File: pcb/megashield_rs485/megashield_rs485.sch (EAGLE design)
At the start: 16 parts

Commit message: PCB template
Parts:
- removed JP10: (no value), SparkFun:M06LOCK
- removed JP11, JP12: (no value), SparkFun:M02LOCK
- removed JP3, JP4, JP5, JP6, JP7: (no value), SparkFun:M08LOCK
- removed JP8, JP9: M16LOCK, SparkFun:M16LOCK
- removed LED1: Red, SparkFun:LED5MM
- removed LED2: Green, SparkFun:LED5MM
- removed R1, R2: 330, SparkFun:RESISTORPTH1
- removed R3: 10k, SparkFun:RESISTORPTH1
- removed S1: (no value), SparkFun:TAC_SWITCHPTH
- added J1, J2, J3, J8, J9: (no value), mecatronica_eagle_lib:M08LONGPADS
- added J10: (no value), mecatronica_eagle_lib:M06LONGPADS
- added J4, J5: (no value), mecatronica_eagle_lib:M16PTH
- added J6, J7: (no value), mecatronica_eagle_lib:M02PTH
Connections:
- removed net GND: JP10.4, JP10.5, JP11.1, JP11.2, JP3.7, LED1.C, LED2.C, S1.1, S1.2
- removed net N$126: LED1.A, R1.1
- removed net N$127: LED2.A, R2.1
- new net ASD: J1.7, J10.4, J10.5, J7.1, J7.2
- net 3.3: now also J10.2; no longer JP10.2
- net 5V: now also J10.3; no longer JP10.3, R1.2, R3.2
- net 5V@1: now also J6.1, J6.2; no longer JP12.1, JP12.2
- net A0: now also J9.1; no longer JP7.1
- net A1: now also J9.2; no longer JP7.2
- net A10: now also J8.3; no longer JP6.3
- net A11: now also J8.4; no longer JP6.4
- net A12: now also J8.5; no longer JP6.5
- net A13: now also J8.6; no longer JP6.6
- net A14: now also J8.7; no longer JP6.7
- net A15: now also J8.8; no longer JP6.8
- net A2: now also J9.3; no longer JP7.3
- net A3: now also J9.4; no longer JP7.4
- net A4: now also J9.5; no longer JP7.5
- net A5: now also J9.6; no longer JP7.6
- net A6: now also J9.7; no longer JP7.7
- net A7: now also J9.8; no longer JP7.8
- net A8: now also J8.1; no longer JP6.1
- net A9: now also J8.2; no longer JP6.2
- net AREF: now also J1.8; no longer JP3.8
- net D10: now also J1.3; no longer JP3.3
- net D11: now also J1.4; no longer JP3.4
- net D12: now also J1.5; no longer JP3.5
- net D13: now also J1.6; no longer JP3.6, R2.2
- net D14: now also J3.8; no longer JP5.8
- net D15: now also J3.7; no longer JP5.7
- net D16: now also J3.6; no longer JP5.6
- net D17: now also J3.5; no longer JP5.5
- net D18: now also J3.4; no longer JP5.4
- net D19: now also J3.3; no longer JP5.3
- net D2: now also J2.3; no longer JP4.3
- net D22: now also J5.1; no longer JP9.1
- net D23: now also J4.16; no longer JP8.16
- net D24: now also J5.2; no longer JP9.2
- net D25: now also J4.15; no longer JP8.15
- net D26: now also J5.3; no longer JP9.3
- net D27: now also J4.14; no longer JP8.14
- net D28: now also J5.4; no longer JP9.4
- net D29: now also J4.13; no longer JP8.13
- net D3: now also J2.4; no longer JP4.4
- net D30: now also J5.5; no longer JP9.5
- net D31: now also J4.12; no longer JP8.12
- net D32: now also J5.6; no longer JP9.6
- net D33: now also J4.11; no longer JP8.11
- net D34: now also J5.7; no longer JP9.7
- net D35: now also J4.10; no longer JP8.10
- net D36: now also J5.8; no longer JP9.8
- net D37: now also J4.9; no longer JP8.9
- net D38: now also J5.9; no longer JP9.9
- net D39: now also J4.8; no longer JP8.8
- net D4: now also J2.5; no longer JP4.5
- net D40: now also J5.10; no longer JP9.10
- net D41: now also J4.7; no longer JP8.7
- net D42: now also J5.11; no longer JP9.11
- net D43: now also J4.6; no longer JP8.6
- net D44: now also J5.12; no longer JP9.12
- net D45: now also J4.5; no longer JP8.5
- net D46: now also J5.13; no longer JP9.13
- net D47: now also J4.4; no longer JP8.4
- net D48: now also J5.14; no longer JP9.14
- net D49: now also J4.3; no longer JP8.3
- net D5: now also J2.6; no longer JP4.6
- net D50: now also J5.15; no longer JP9.15
- net D51: now also J4.2; no longer JP8.2
- net D52: now also J5.16; no longer JP9.16
- net D53: now also J4.1; no longer JP8.1
- net D6: now also J2.7; no longer JP4.7
- net D7: now also J2.8; no longer JP4.8
- net D8: now also J1.1; no longer JP3.1
- net D9: now also J1.2; no longer JP3.2
- net RES: now also J10.1; no longer JP10.1, R3.1, S1.3, S1.4
- net RX0: now also J2.1; no longer JP4.1
- net SCL: now also J3.1; no longer JP5.1
- net SDA: now also J3.2; no longer JP5.2
- net TX1: now also J2.2; no longer JP4.2
- net VIN: now also J10.6; no longer JP10.6

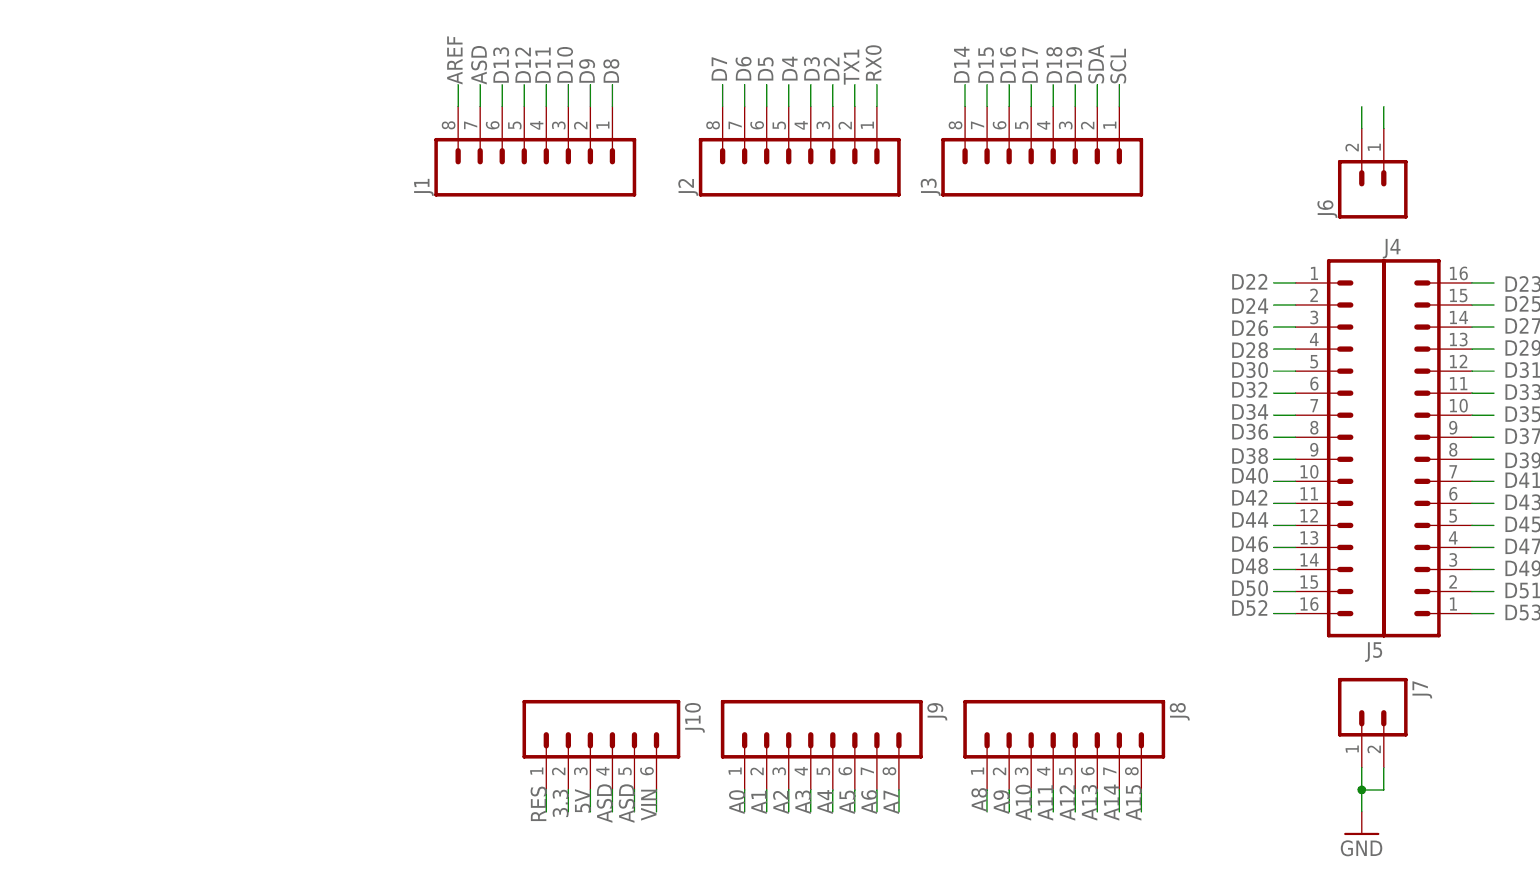
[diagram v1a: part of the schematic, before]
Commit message: Add rs485 transceiver
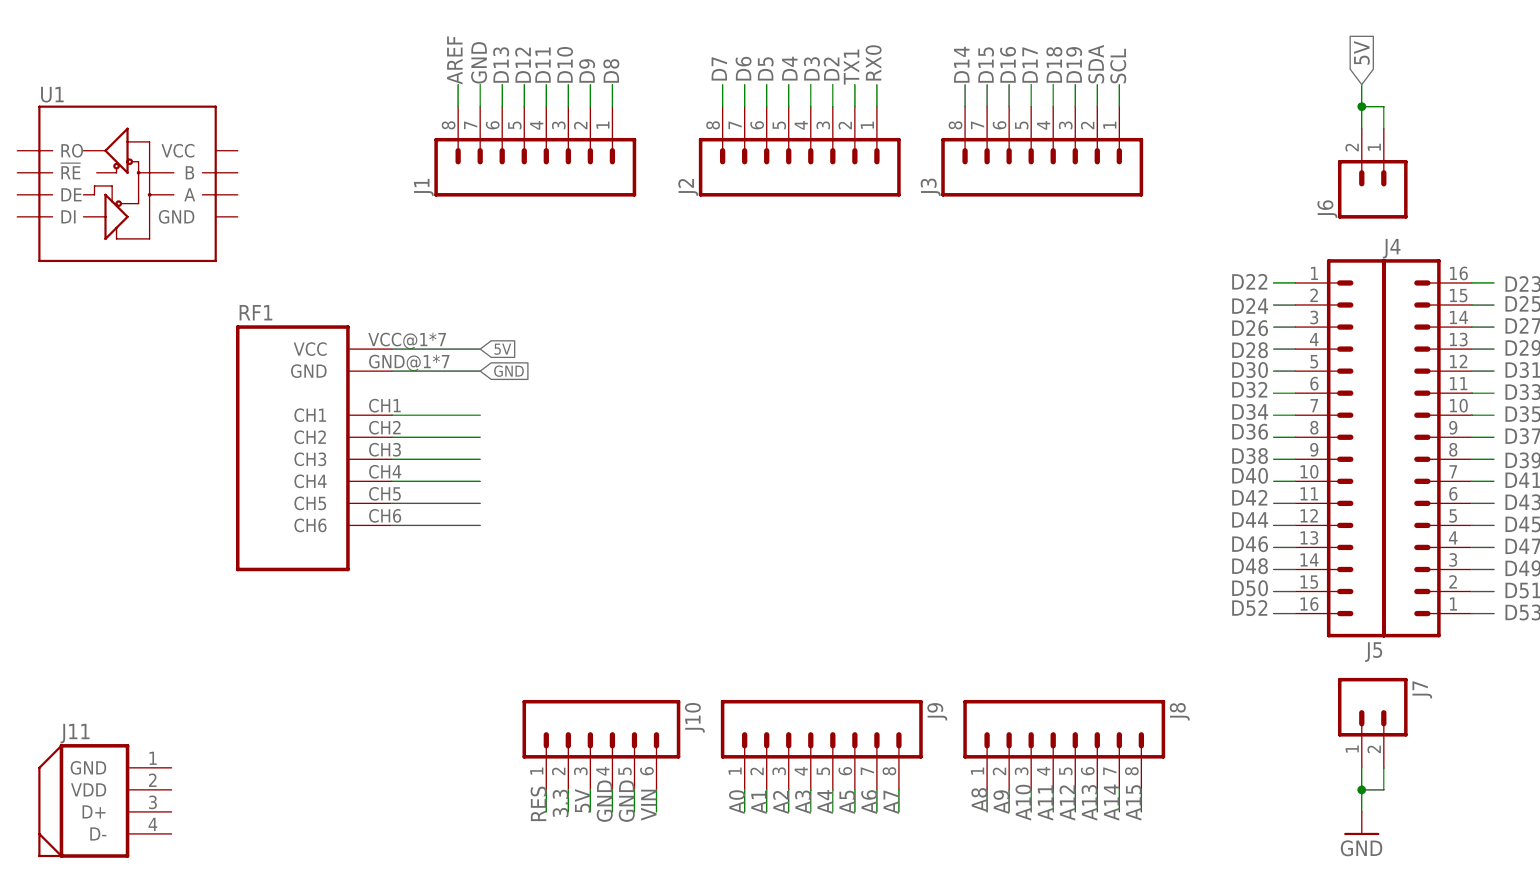
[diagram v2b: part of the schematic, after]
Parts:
- added J11: DYNAMIXEL_RS485, mecatronica_eagle_lib:DYNAMIXEL_RS485
- added RF1: FS_R6B, mecatronica_eagle_lib:FS_R6B
- added U1: SN75176B, mecatronica_eagle_lib:SN75176B
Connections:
- removed net 5V@1: J6.1, J6.2
- removed net ASD: J1.7, J10.4, J10.5, J7.1, J7.2
- new net GND: J1.7, J10.4, J10.5, J7.1, J7.2, RF1.GND
- new net N$3: RF1.CH1
- new net N$4: RF1.CH2
- new net N$5: RF1.CH3
- new net N$6: RF1.CH4
- new net N$7: RF1.CH5
- new net N$8: RF1.CH6
- net 5V: now also J6.1, J6.2, RF1.VCC

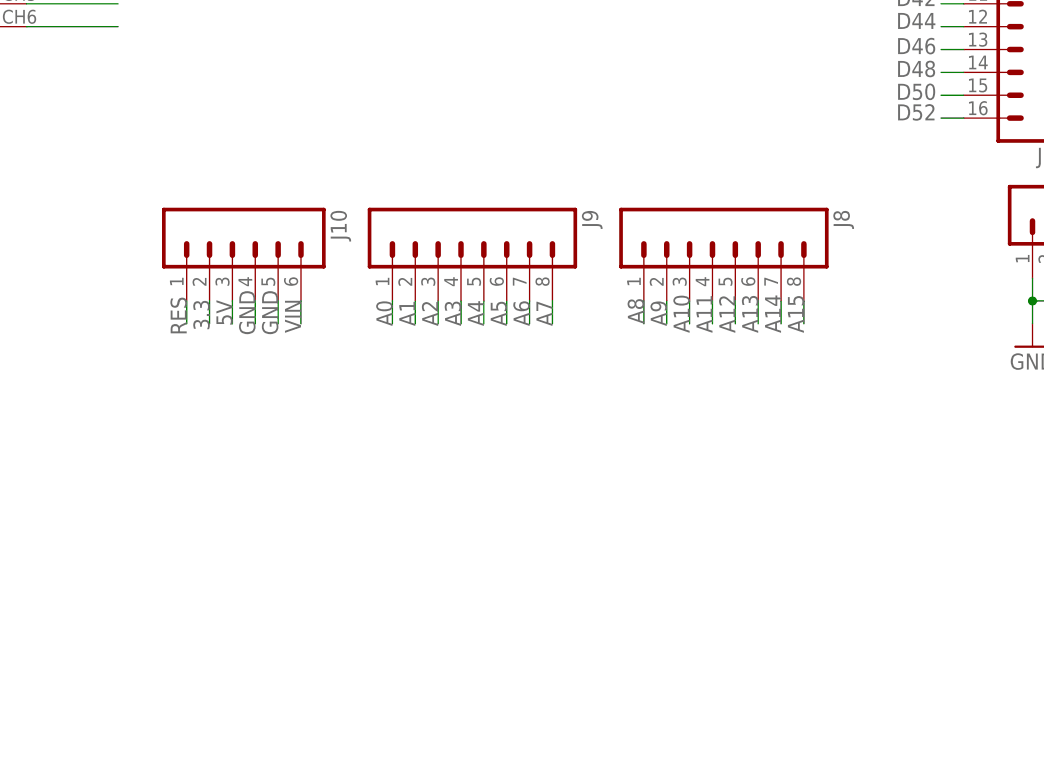
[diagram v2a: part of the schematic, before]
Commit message: Add analog inputs
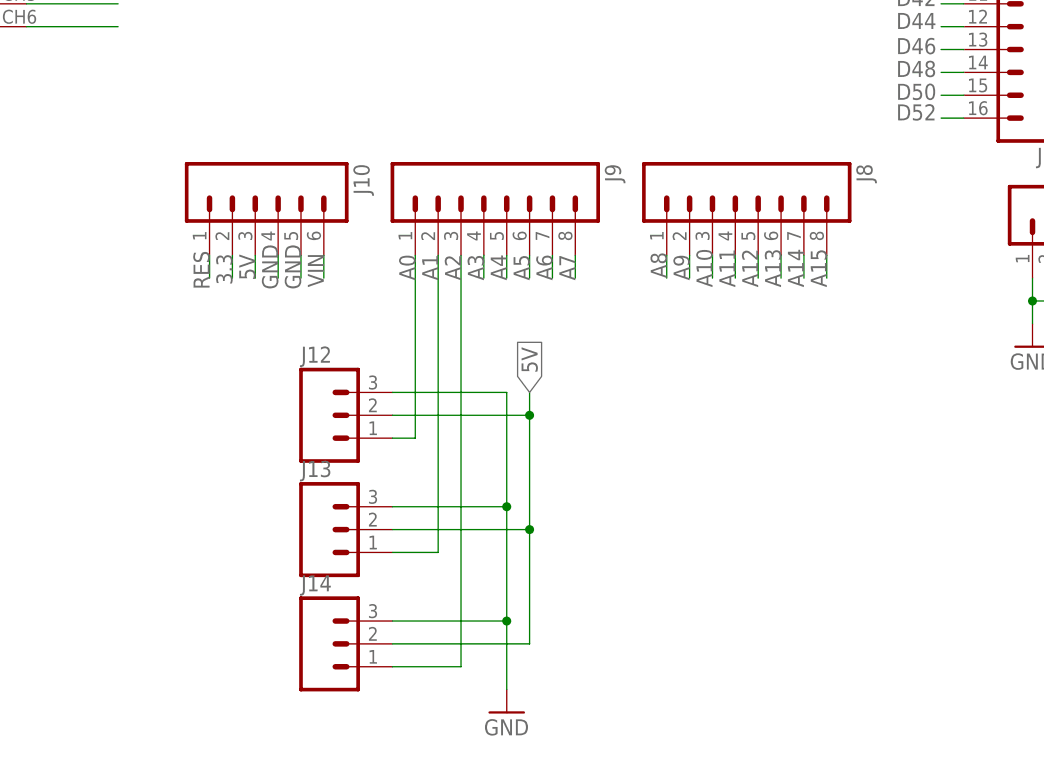
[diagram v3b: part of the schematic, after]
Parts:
- added J12, J13, J14: (no value), mecatronica_eagle_lib:M03LONGPADS
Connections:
- net 5V: now also J12.2, J13.2, J14.2
- net A0: now also J12.1
- net A1: now also J13.1
- net A2: now also J14.1
- net GND: now also J12.3, J13.3, J14.3
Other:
- moved on the sheet: J10, J8, J9
